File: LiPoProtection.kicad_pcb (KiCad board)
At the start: 2 copper layers, 50 x 50 mm, 51 parts, among them P1 CONN_01X05, P2 Load, P3 Supply, Q1 IRLML2502, U1 LM324, U2 LM324, U3 74HC08, U4 LP2950

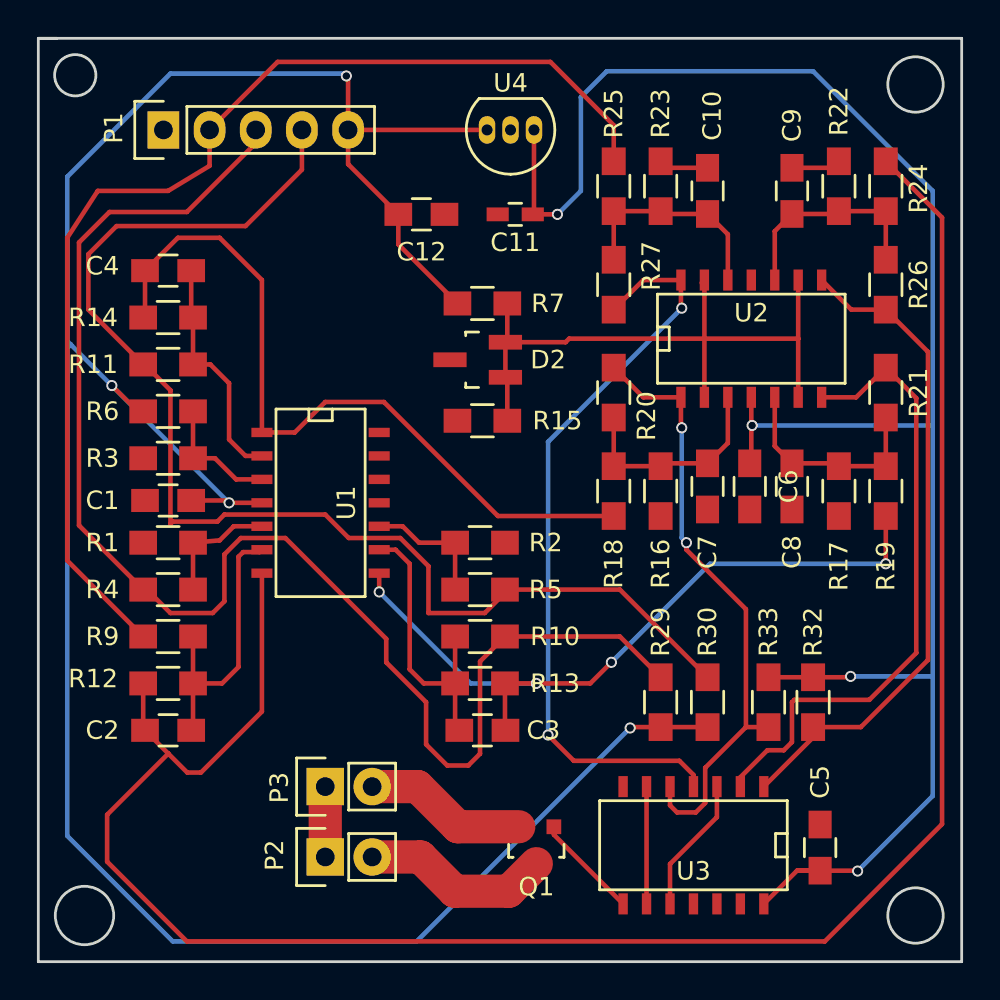
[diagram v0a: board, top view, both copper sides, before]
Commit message: Added mass areas
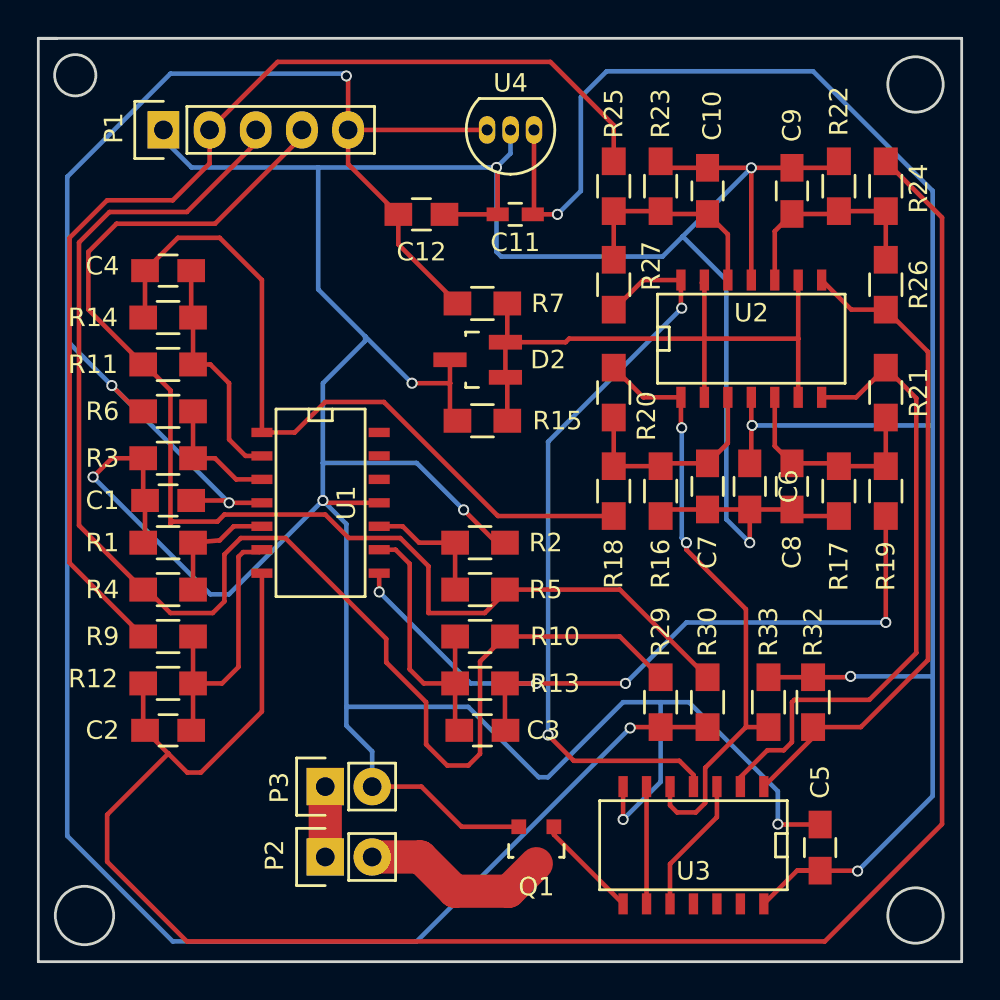
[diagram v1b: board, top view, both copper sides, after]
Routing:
- net GND: track 14.3 -> 229.5 mm, vias 0 -> 9
- net Net-(C3-Pad1): track 40.0 -> 41.9 mm
- net Net-(P1-Pad4): track 67.7 -> 66.7 mm
- added copper zone on B.Cu, net GND
- added copper zone on F.Cu, net GND

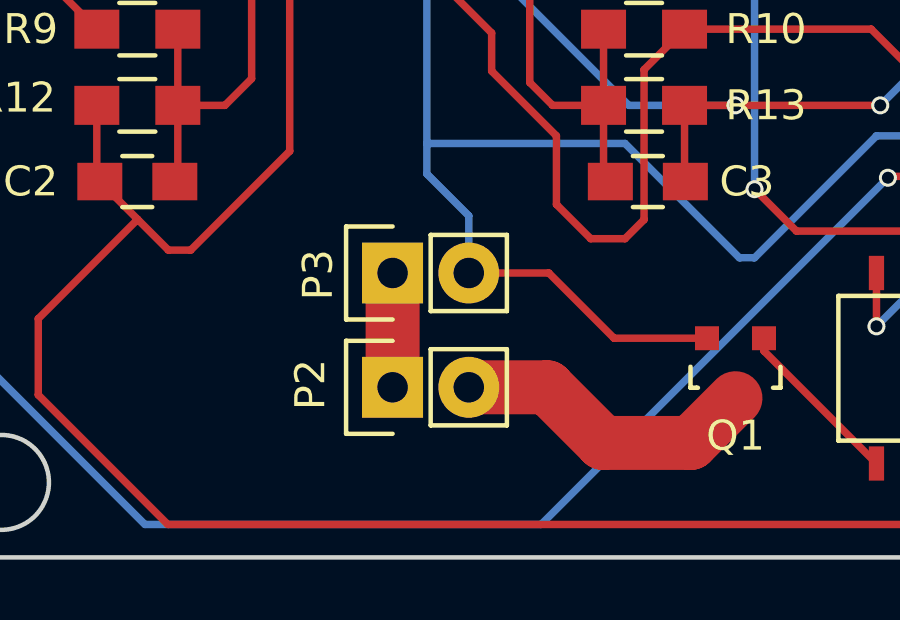
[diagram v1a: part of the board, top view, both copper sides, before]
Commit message: Moved supply and load pins
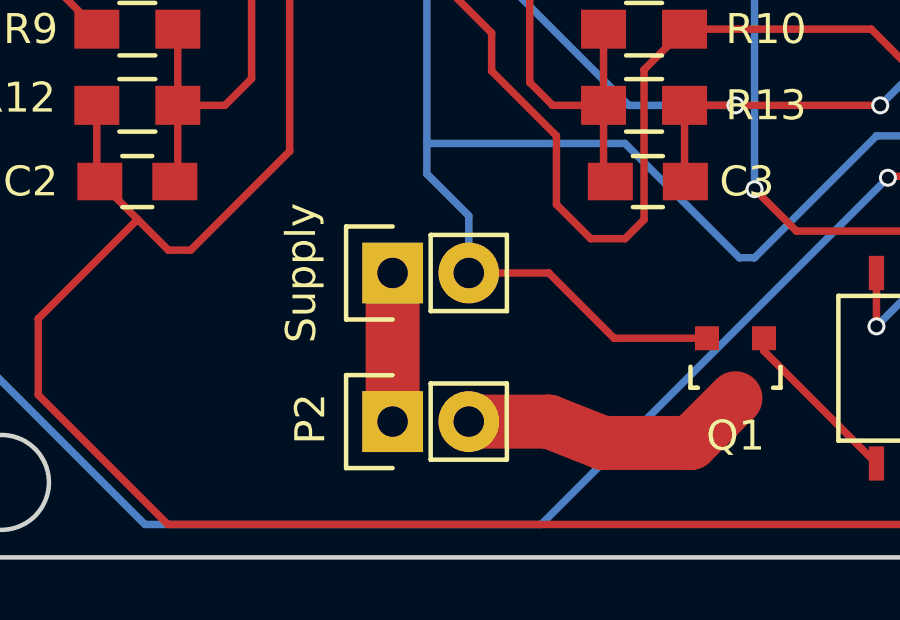
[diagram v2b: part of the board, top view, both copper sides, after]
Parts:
- moved P2 1.14 mm to (105.5, 101.5)
- renumbered P3 to Supply
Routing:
- net Net-(P2-Pad1): track 3.81 -> 4.95 mm
- net Net-(P2-Pad2): track 10.3 -> 9.64 mm
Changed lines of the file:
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@@
     (links 109)
     (no_connects 0)
-    (area 89.924999 55.924999 140.075001 106.075001)
+    (area 70.000001 40.65 140.075001 106.075001)
     (thickness 1.6)
     (drawings 11)
@@
   )
   (module Pin_Headers:Pin_Header_Straight_1x02 (layer F.Cu)
-    (at 105.537 100.33 90)
+    (at 105.537 101.473 90)
     (descr "Through hole pin header")
     (tags "pin header")
@@
     (descr "Through hole pin header")
     (tags "pin header")
-    (fp_text reference P3 (at -0.058 -2.488 90) (layer F.SilkS)
+    (fp_text reference Supply (at 0 -3.048 90) (layer F.SilkS)
       (effects (font (size 1 1) (thickness 0.15)))
     )
@@
   (segment (start 116.84 65.598) (end 116.84 60.96) (width 0.25) (layer F.Cu) (net 2) (status 30))
   (segment (start 116.774 61.026) (end 116.84 60.96) (width 0.25) (layer F.Cu) (net 2) (status 30))
-  (segment (start 105.537 96.52) (end 105.537 100.33) (width 1.8) (layer F.Cu) (net 3))
+  (segment (start 105.537 96.52) (end 105.537 101.473) (width 1.8) (layer F.Cu) (net 3) (status 20))
   (segment (start 115.47602 102.1842) (end 116.967 100.69322) (width 1.8) (layer F.Cu) (net 4))
+  (segment (start 108.077 101.473) (end 110.744 101.473) (width 1.8) (layer F.Cu) (net 4) (status 10))
+  (segment (start 110.744 101.473) (end 112.5474 102.1842) (width 1.8) (layer F.Cu) (net 4))
   (segment (start 112.5474 102.1842) (end 115.47602 102.1842) (width 1.8) (layer F.Cu) (net 4))
-  (segment (start 110.6932 100.33) (end 112.5474 102.1842) (width 1.8) (layer F.Cu) (net 4))
-  (segment (start 108.077 100.33) (end 110.6932 100.33) (width 1.8) (layer F.Cu) (net 4))
   (segment (start 98.378 83.312) (end 98.378 85.852) (width 0.25) (layer F.Cu) (net 5) (status 30))
   (segment (start 98.378 83.312) (end 99.822 83.185) (width 0.25) (layer F.Cu) (net 5) (status 10))
